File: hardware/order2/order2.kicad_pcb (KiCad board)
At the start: 2 copper layers, 377.8 x 228.9 mm, 183 parts, among them IC1 ATMEGA88-A, IC1 ATMEGA88A-A, J1 RJ45, J1 RJ45_8P8C_8FACH, K1 CONN_3, K1 pow_sel, K2 CONN_3, P1 CONN_4, P1 CONN_8, P1 ISP, P1 UART, P10 CONN_10, P11 CONN_8, P2 CONN_4, P2 CONN_6, P2 Shield, P2 UART, P2 so8, P3 CONN_4, P3 CONN_6, P3 i2c_pow, P4 CONN_8, P4 i2c_chain, P5 12Vin, P5 POW, P6 HOHLBUCHSE, P6 TWI, P7 TWI_POW, P7 Vccin, P8 CONN_10, P8 ISP, P9 5Vin, P9 CONN_8, SW1 SW1, SW1 SW_RESET, SW2 SCHALTER_2POL, SW3 SW_RESET, U1 LM7805, U1 ST485, U1 TSIC50XF, U2 HYT271, U2 ST485, U3 ST485, U4 ST485, U5 ST485, U6 ST485, U7 ST485, U8 ST485, U9 ST485, X1 20MHz, m3_loch VAL**

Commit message: humidity in place
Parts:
- moved C1 127.0 mm to (178.5, 119.6)
- moved C2 127.0 mm to (193.5, 132.5)
- moved C3 127.0 mm to (180.5, 135.8)
- moved C4 127.0 mm to (193.5, 135.5)
- moved C5 127.0 mm to (187.0, 141.0)
- moved C6 127.0 mm to (179.0, 103.0)
- moved D1 127.0 mm to (192.5, 112.9)
- moved IC1 127.0 mm to (184.5, 114.5)
- moved J1 127.0 mm to (186.5, 153.5)
- moved P1 127.0 mm to (186.5, 125.5)
- moved P2 127.0 mm to (180.7, 105.1)
- moved R1 127.0 mm to (192.5, 117.5)
- moved R3 127.0 mm to (180.5, 132.2)
- moved R4 127.0 mm to (180.5, 138.8)
- moved R5 127.0 mm to (193.5, 138.5)
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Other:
- board size 377.8 x 228.9 mm -> 381.8 x 229.9 mm

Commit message: 2 temp boards
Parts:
- added C1: 100nF, SM0603_big, F.Cu at (315.2, 203.0)
- added C2: 100nF, SM0603_big, F.Cu at (329.8, 211.8)
- added C3: 10uF, SM0805_big, F.Cu at (329.8, 215.2)
- added C4: 100nF, SM0603_big, F.Cu at (324.2, 222.5)
- added J1: RJ45, RJ45_8P8_simple, F.Cu at (322.5, 228.5)
- added R1: 220, SM0603_big, F.Cu at (315.2, 207.0)
- added R2: 22k, SM0603_big, F.Cu at (325.0, 218.8)
- added R3: 22k, SM0603_big, F.Cu at (330.0, 218.8)
- added R4: 120, SM0603_big, F.Cu at (328.2, 222.5)
- added U1: TSIC50XF, Tsic_TO92, F.Cu at (322.5, 172.0)
- added U2: ST485, st485, F.Cu at (322.5, 212.8)
- added m3_loch: VAL**, m3_loch, F.Cu at (327.5, 204.2)
- added m3_loch: VAL**, m3_loch, F.Cu at (317.5, 220.2)
- moved K1 389.8 mm to (40.7, 269.5)
- moved K2 389.8 mm to (35.6, 269.5)
- moved P1 389.8 mm to (48.7, 235.3)
- moved P1 389.8 mm to (33.7, 236.3)
- moved P1 389.8 mm to (61.2, 266.3)
- moved P2 389.8 mm to (48.7, 230.9)
- moved P2 389.8 mm to (33.7, 231.9)
- moved P2 389.8 mm to (66.3, 266.3)
- moved P3 389.8 mm to (48.7, 222.6)
- moved P3 389.8 mm to (33.7, 223.6)
- moved C1 273.9 mm to (311.2, 73.5), turned to 270 degrees
- moved R1 273.4 mm to (311.2, 69.5), turned to 270 degrees
- moved U1 271.7 mm to (304.0, 104.5), turned to 0 degrees
- moved m3_loch 269.4 mm to (309.0, 56.2), turned to 90 degrees
- moved U2 262.7 mm to (304.0, 63.8), turned to 45 degrees
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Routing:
- net GND: track 1547.1 -> 1674.0 mm, vias 17 -> 19
- net VCC: track 1094.8 -> 1152.5 mm, vias 10 -> 13
- net N-000007: track 59.1 -> 104.6 mm
- net N-0000010: track 42.9 -> 82.4 mm
- net /zb: track 80.3 -> 105.2 mm
- net /za: track 82.4 -> 106.6 mm
- net N-000003: track 24.9 -> 27.0 mm
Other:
- board size 381.8 x 229.9 mm -> 312.5 x 247.6 mm

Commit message: 10 temp sensor work
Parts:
- added C1: 100nF, SM0603_big, F.Cu at (318.2, 68.5)
- added C1: 100nF, SM0603_big, F.Cu at (288.8, 79.5)
- added C1: 100nF, SM0603_big, F.Cu at (318.8, 79.5)
- added C1: 100nF, SM0603_big, F.Cu at (348.2, 68.5)
- added C1: 100nF, SM0603_big, F.Cu at (288.2, 68.5)
- added C1: 100nF, SM0603_big, F.Cu at (258.8, 79.5)
- added C1: 100nF, SM0603_big, F.Cu at (378.2, 68.5)
- added C1: 100nF, SM0603_big, F.Cu at (348.8, 79.5)
- added C2: 100nF, SM0603_big, F.Cu at (303.8, 59.8)
- added C2: 100nF, SM0603_big, F.Cu at (303.2, 88.2)
- added C2: 100nF, SM0603_big, F.Cu at (333.2, 88.2)
- added C2: 100nF, SM0603_big, F.Cu at (333.8, 59.8)
- added C2: 100nF, SM0603_big, F.Cu at (273.8, 59.8)
- added C2: 100nF, SM0603_big, F.Cu at (273.2, 88.2)
- added C2: 100nF, SM0603_big, F.Cu at (363.8, 59.8)
- added C2: 100nF, SM0603_big, F.Cu at (363.2, 88.2)
- added C3: 10uF, SM0805_big, F.Cu at (303.8, 56.2)
- added C3: 10uF, SM0805_big, F.Cu at (303.2, 91.8)
- added C3: 10uF, SM0805_big, F.Cu at (333.2, 91.8)
- added C3: 10uF, SM0805_big, F.Cu at (333.8, 56.2)
- added C3: 10uF, SM0805_big, F.Cu at (273.8, 56.2)
- added C3: 10uF, SM0805_big, F.Cu at (273.2, 91.8)
- added C3: 10uF, SM0805_big, F.Cu at (363.8, 56.2)
- added C3: 10uF, SM0805_big, F.Cu at (363.2, 91.8)
- added C4: 100nF, SM0603_big, F.Cu at (309.2, 49.0)
- added C4: 100nF, SM0603_big, F.Cu at (297.8, 99.0)
- added C4: 100nF, SM0603_big, F.Cu at (327.8, 99.0)
- added C4: 100nF, SM0603_big, F.Cu at (339.2, 49.0)
- added C4: 100nF, SM0603_big, F.Cu at (279.2, 49.0)
- added C4: 100nF, SM0603_big, F.Cu at (267.8, 99.0)
- added C4: 100nF, SM0603_big, F.Cu at (369.2, 49.0)
- added C4: 100nF, SM0603_big, F.Cu at (357.8, 99.0)
- added J1: RJ45, RJ45_8P8_simple, F.Cu at (311.0, 43.0)
- added J1: RJ45, RJ45_8P8_simple, F.Cu at (296.0, 105.0)
- added J1: RJ45, RJ45_8P8_simple, F.Cu at (326.0, 105.0)
- added J1: RJ45, RJ45_8P8_simple, F.Cu at (341.0, 43.0)
- added J1: RJ45, RJ45_8P8_simple, F.Cu at (281.0, 43.0)
- added J1: RJ45, RJ45_8P8_simple, F.Cu at (266.0, 105.0)
- added J1: RJ45, RJ45_8P8_simple, F.Cu at (371.0, 43.0)
- added J1: RJ45, RJ45_8P8_simple, F.Cu at (356.0, 105.0)
- added R1: 220, SM0603_big, F.Cu at (318.2, 64.5)
- added R1: 220, SM0603_big, F.Cu at (288.8, 83.5)
- added R1: 220, SM0603_big, F.Cu at (318.8, 83.5)
- added R1: 220, SM0603_big, F.Cu at (348.2, 64.5)
- added R1: 220, SM0603_big, F.Cu at (288.2, 64.5)
- added R1: 220, SM0603_big, F.Cu at (258.8, 83.5)
- added R1: 220, SM0603_big, F.Cu at (378.2, 64.5)
- added R1: 220, SM0603_big, F.Cu at (348.8, 83.5)
- added R2: 22k, SM0603_big, F.Cu at (308.5, 52.8)
- added R2: 22k, SM0603_big, F.Cu at (298.5, 95.2)
- added R2: 22k, SM0603_big, F.Cu at (328.5, 95.2)
- added R2: 22k, SM0603_big, F.Cu at (338.5, 52.8)
- added R2: 22k, SM0603_big, F.Cu at (278.5, 52.8)
- added R2: 22k, SM0603_big, F.Cu at (268.5, 95.2)
- added R2: 22k, SM0603_big, F.Cu at (368.5, 52.8)
- added R2: 22k, SM0603_big, F.Cu at (358.5, 95.2)
- added R3: 22k, SM0603_big, F.Cu at (303.5, 52.8)
- added R3: 22k, SM0603_big, F.Cu at (303.5, 95.2)
- added R3: 22k, SM0603_big, F.Cu at (333.5, 95.2)
- added R3: 22k, SM0603_big, F.Cu at (333.5, 52.8)
- added R3: 22k, SM0603_big, F.Cu at (273.5, 52.8)
- added R3: 22k, SM0603_big, F.Cu at (273.5, 95.2)
- added R3: 22k, SM0603_big, F.Cu at (363.5, 52.8)
- added R3: 22k, SM0603_big, F.Cu at (363.5, 95.2)
- added R4: 120, SM0603_big, F.Cu at (305.2, 49.0)
- added R4: 120, SM0603_big, F.Cu at (301.8, 99.0)
- added R4: 120, SM0603_big, F.Cu at (331.8, 99.0)
- added R4: 120, SM0603_big, F.Cu at (335.2, 49.0)
- added R4: 120, SM0603_big, F.Cu at (275.2, 49.0)
- added R4: 120, SM0603_big, F.Cu at (271.8, 99.0)
- added R4: 120, SM0603_big, F.Cu at (365.2, 49.0)
- added R4: 120, SM0603_big, F.Cu at (361.8, 99.0)
- added U1: TSIC50XF, Tsic_TO92, F.Cu at (311.0, 99.5)
- added U1: TSIC50XF, Tsic_TO92, F.Cu at (296.0, 48.5)
- added U1: TSIC50XF, Tsic_TO92, F.Cu at (326.0, 48.5)
- added U1: TSIC50XF, Tsic_TO92, F.Cu at (341.0, 99.5)
- added U1: TSIC50XF, Tsic_TO92, F.Cu at (281.0, 99.5)
- added U1: TSIC50XF, Tsic_TO92, F.Cu at (266.0, 48.5)
- added U1: TSIC50XF, Tsic_TO92, F.Cu at (371.0, 99.5)
- added U1: TSIC50XF, Tsic_TO92, F.Cu at (356.0, 48.5)
- added U2: ST485, st485, F.Cu at (311.0, 58.8)
- added U2: ST485, st485, F.Cu at (296.0, 89.2)
- added U2: ST485, st485, F.Cu at (326.0, 89.2)
- added U2: ST485, st485, F.Cu at (341.0, 58.8)
- added U2: ST485, st485, F.Cu at (281.0, 58.8)
- added U2: ST485, st485, F.Cu at (266.0, 89.2)
- added U2: ST485, st485, F.Cu at (371.0, 58.8)
- added U2: ST485, st485, F.Cu at (356.0, 89.2)
- added m3_loch: VAL**, m3_loch, F.Cu at (306.0, 67.2)
- added m3_loch: VAL**, m3_loch, F.Cu at (286.0, 51.2)
- added m3_loch: VAL**, m3_loch, F.Cu at (261.0, 96.8)
- added m3_loch: VAL**, m3_loch, F.Cu at (271.0, 80.8)
- added m3_loch: VAL**, m3_loch, F.Cu at (366.0, 67.2)
- added m3_loch: VAL**, m3_loch, F.Cu at (376.0, 51.2)
- added m3_loch: VAL**, m3_loch, F.Cu at (351.0, 96.8)
- added m3_loch: VAL**, m3_loch, F.Cu at (361.0, 80.8)
- added m3_loch: VAL**, m3_loch, F.Cu at (316.0, 51.2)
- added m3_loch: VAL**, m3_loch, F.Cu at (291.0, 96.8)
- added m3_loch: VAL**, m3_loch, F.Cu at (301.0, 80.8)
- added m3_loch: VAL**, m3_loch, F.Cu at (331.0, 80.8)
- added m3_loch: VAL**, m3_loch, F.Cu at (321.0, 96.8)
- added m3_loch: VAL**, m3_loch, F.Cu at (346.0, 51.2)
- added m3_loch: VAL**, m3_loch, F.Cu at (336.0, 67.2)
- added m3_loch: VAL**, m3_loch, F.Cu at (276.0, 67.2)
- moved C1 150.8 mm to (228.8, 79.5)
- moved C2 150.8 mm to (243.2, 88.2)
- moved C3 150.8 mm to (243.2, 91.8)
- moved C4 150.8 mm to (237.8, 99.0)
- moved J1 150.8 mm to (236.0, 105.0)
- moved R1 150.8 mm to (228.8, 83.5)
- moved R2 150.8 mm to (238.5, 95.2)
- moved R3 150.8 mm to (243.5, 95.2)
- moved R4 150.8 mm to (241.8, 99.0)
- moved U1 150.8 mm to (236.0, 48.5)
- moved U2 150.8 mm to (236.0, 89.2)
- moved m3_loch 150.8 mm to (241.0, 80.8)
- moved m3_loch 150.8 mm to (231.0, 96.8)
- moved C1 53.2 mm to (258.2, 68.5)
- moved C2 53.2 mm to (243.8, 59.8)
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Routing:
- net GND: track 1674.0 -> 2688.7 mm, vias 19 -> 35
- net VCC: track 1152.5 -> 1613.9 mm, vias 13 -> 37
- net N-000007: track 104.6 -> 468.9 mm
- net N-0000010: track 82.4 -> 398.4 mm
- net /zb: track 105.2 -> 304.7 mm
- net /za: track 106.6 -> 299.5 mm
- net N-000003: track 27.0 -> 43.9 mm
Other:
- board size 312.5 x 247.6 mm -> 361 x 247.6 mm

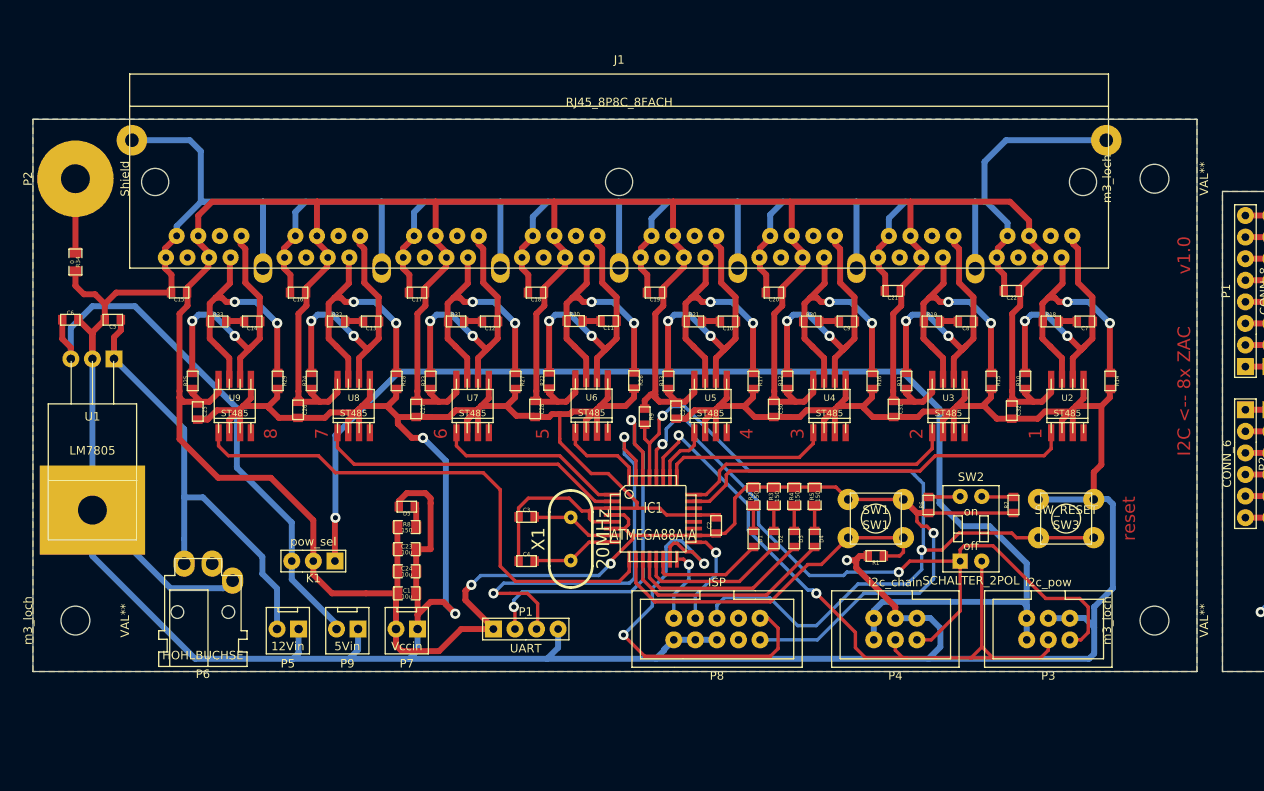
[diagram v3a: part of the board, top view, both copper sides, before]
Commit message: sensor board rotated
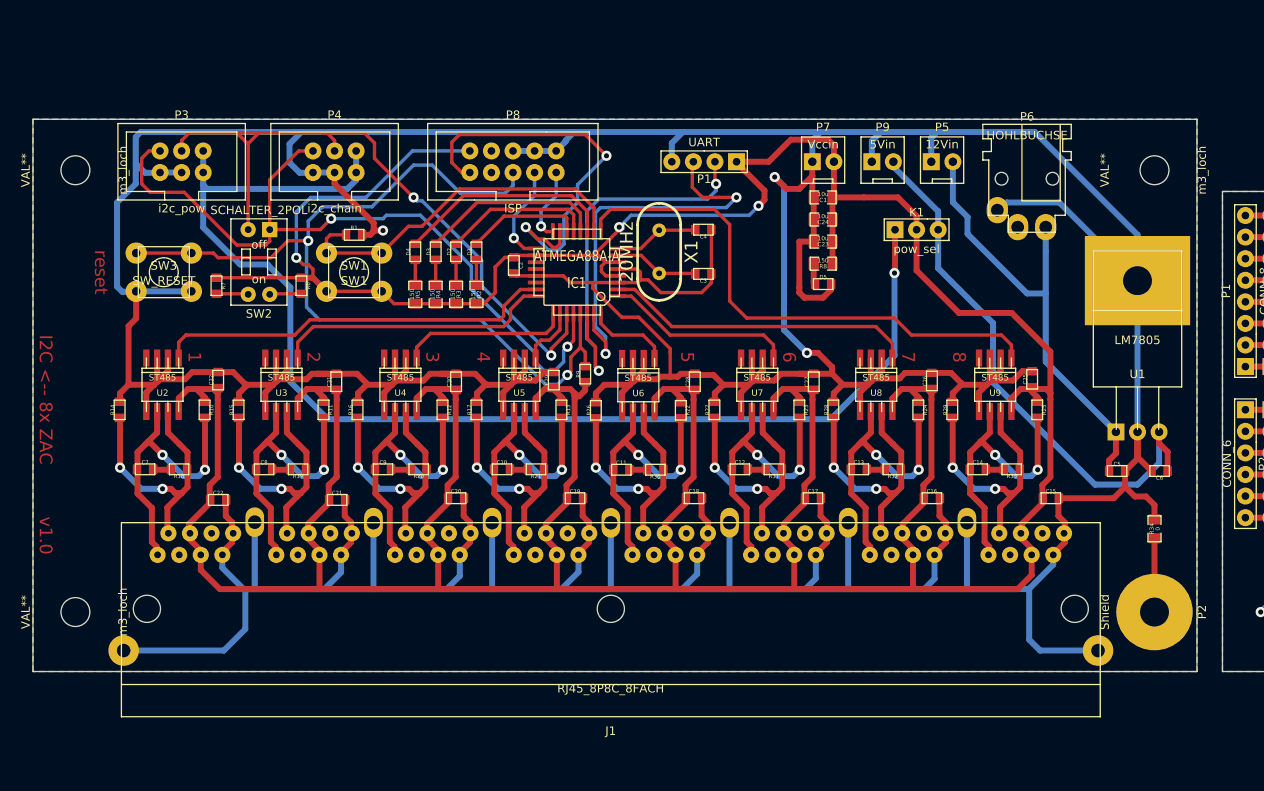
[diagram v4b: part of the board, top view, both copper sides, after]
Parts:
- moved m3_loch 137.6 mm to (25.0, 126.0), turned to 270 degrees
- moved m3_loch 137.6 mm to (152.0, 126.0), turned to 270 degrees
- moved P2 136.9 mm to (152.0, 178.0), turned to 270 degrees
- moved m3_loch 136.9 mm to (25.0, 178.0), turned to 270 degrees
- moved R34 130.8 mm to (152.0, 168.2), turned to 90 degrees
- moved C6 129.4 mm to (152.6, 161.4), turned to 180 degrees
- moved U1 125.9 mm to (150.0, 139.0), turned to 0 degrees
- moved C5 119.5 mm to (147.6, 161.4), turned to 0 degrees
- moved R14 116.6 mm to (30.2, 154.2), turned to 90 degrees
- moved P3 115.9 mm to (37.5, 125.0), turned to 0 degrees
- moved C7 112.0 mm to (33.2, 161.2), turned to 0 degrees
- moved SW3 110.1 mm to (35.4, 138.0), turned to 0 degrees
- moved P6 109.6 mm to (137.0, 127.0), turned to 0 degrees
- moved U2 106.5 mm to (35.2, 153.2), turned to 180 degrees
- moved C15 105.4 mm to (139.8, 164.6), turned to 0 degrees
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
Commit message: einzeln
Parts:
- removed the C1 at (318.2, 68.5)
- removed the C1 at (288.8, 79.5)
- removed the C1 at (318.8, 79.5)
- removed the C1 at (348.2, 68.5)
- removed the C1 at (288.2, 68.5)
- removed the C1 at (258.8, 79.5)
- removed the C1 at (378.2, 68.5)
- removed the C1 at (348.8, 79.5)
- removed the C2 at (303.8, 59.8)
- removed the C2 at (303.2, 88.2)
- removed the C2 at (333.2, 88.2)
- removed the C2 at (333.8, 59.8)
- removed the C2 at (273.8, 59.8)
- removed the C2 at (273.2, 88.2)
- removed the C2 at (363.8, 59.8)
- removed the C2 at (363.2, 88.2)
- removed the C3 at (303.8, 56.2)
- removed the C3 at (303.2, 91.8)
- removed the C3 at (333.2, 91.8)
- removed the C3 at (333.8, 56.2)
- removed the C3 at (273.8, 56.2)
- removed the C3 at (273.2, 91.8)
- removed the C3 at (363.8, 56.2)
- removed the C3 at (363.2, 91.8)
- removed the C4 at (309.2, 49.0)
- removed the C4 at (297.8, 99.0)
- removed the C4 at (327.8, 99.0)
- removed the C4 at (339.2, 49.0)
- removed the C4 at (279.2, 49.0)
- removed the C4 at (267.8, 99.0)
- removed the C4 at (369.2, 49.0)
- removed the C4 at (357.8, 99.0)
- removed the J1 at (311.0, 43.0)
- removed the J1 at (296.0, 105.0)
- removed the J1 at (326.0, 105.0)
- removed the J1 at (341.0, 43.0)
- removed the J1 at (281.0, 43.0)
- removed the J1 at (266.0, 105.0)
- removed the J1 at (371.0, 43.0)
- removed the J1 at (356.0, 105.0)
- removed the R1 at (318.2, 64.5)
- removed the R1 at (288.8, 83.5)
- removed the R1 at (318.8, 83.5)
- removed the R1 at (348.2, 64.5)
- removed the R1 at (288.2, 64.5)
- removed the R1 at (258.8, 83.5)
- removed the R1 at (378.2, 64.5)
- removed the R1 at (348.8, 83.5)
- removed the R2 at (308.5, 52.8)
- removed the R2 at (298.5, 95.2)
- removed the R2 at (328.5, 95.2)
- removed the R2 at (338.5, 52.8)
- removed the R2 at (278.5, 52.8)
- removed the R2 at (268.5, 95.2)
- removed the R2 at (368.5, 52.8)
- removed the R2 at (358.5, 95.2)
- removed the R3 at (303.5, 52.8)
- removed the R3 at (303.5, 95.2)
- removed the R3 at (333.5, 95.2)
- removed the R3 at (333.5, 52.8)
- removed the R3 at (273.5, 52.8)
- removed the R3 at (273.5, 95.2)
- removed the R3 at (363.5, 52.8)
- removed the R3 at (363.5, 95.2)
- removed the R4 at (305.2, 49.0)
- removed the R4 at (301.8, 99.0)
- removed the R4 at (331.8, 99.0)
- removed the R4 at (335.2, 49.0)
- removed the R4 at (275.2, 49.0)
- removed the R4 at (271.8, 99.0)
- removed the R4 at (365.2, 49.0)
- removed the R4 at (361.8, 99.0)
- removed the U1 at (311.0, 99.5)
- removed the U1 at (296.0, 48.5)
- removed the U1 at (326.0, 48.5)
- removed the U1 at (341.0, 99.5)
- removed the U1 at (281.0, 99.5)
- removed the U1 at (266.0, 48.5)
- removed the U1 at (371.0, 99.5)
- removed the U1 at (356.0, 48.5)
- removed the U2 at (311.0, 58.8)
- removed the U2 at (296.0, 89.2)
- removed the U2 at (326.0, 89.2)
- removed the U2 at (341.0, 58.8)
- removed the U2 at (281.0, 58.8)
- removed the U2 at (266.0, 89.2)
- removed the U2 at (371.0, 58.8)
- removed the U2 at (356.0, 89.2)
- removed the m3_loch at (306.0, 67.2)
- removed the m3_loch at (286.0, 51.2)
- removed the m3_loch at (261.0, 96.8)
- removed the m3_loch at (271.0, 80.8)
- removed the m3_loch at (366.0, 67.2)
- removed the m3_loch at (376.0, 51.2)
- removed the m3_loch at (351.0, 96.8)
- removed the m3_loch at (361.0, 80.8)
- removed the m3_loch at (316.0, 51.2)
- removed the m3_loch at (291.0, 96.8)
- removed the m3_loch at (301.0, 80.8)
- removed the m3_loch at (331.0, 80.8)
- removed the m3_loch at (321.0, 96.8)
- removed the m3_loch at (346.0, 51.2)
- removed the m3_loch at (336.0, 67.2)
- removed the m3_loch at (276.0, 67.2)
- added C1: 100nF, SM0603_big, F.Cu at (181.2, 63.5)
- added C1: 100nF, SM0603_big, F.Cu at (151.8, 74.5)
- added C2: 100nF, SM0603_big, F.Cu at (166.8, 54.8)
- added C2: 100nF, SM0603_big, F.Cu at (166.2, 83.2)
- added C3: 10uF, SM0805_big, F.Cu at (166.8, 51.2)
- added C3: 10uF, SM0805_big, F.Cu at (166.2, 86.8)
- added C4: 100nF, SM0603_big, F.Cu at (172.2, 44.0)
- added C4: 100nF, SM0603_big, F.Cu at (160.8, 94.0)
- added J1: RJ45, RJ45_8P8_simple, F.Cu at (174.0, 38.0)
- added J1: RJ45, RJ45_8P8_simple, F.Cu at (159.0, 100.0)
- added R1: 220, SM0603_big, F.Cu at (181.2, 59.5)
- added R1: 220, SM0603_big, F.Cu at (151.8, 78.5)
- added R2: 22k, SM0603_big, F.Cu at (171.5, 47.8)
- added R2: 22k, SM0603_big, F.Cu at (161.5, 90.2)
- added R3: 22k, SM0603_big, F.Cu at (166.5, 47.8)
- added R3: 22k, SM0603_big, F.Cu at (166.5, 90.2)
- added R4: 120, SM0603_big, F.Cu at (168.2, 44.0)
- added R4: 120, SM0603_big, F.Cu at (164.8, 94.0)
- added U1: TSIC50XF, Tsic_TO92, F.Cu at (174.0, 94.5)
- added U1: TSIC50XF, Tsic_TO92, F.Cu at (159.0, 43.5)
- added U2: ST485, st485, F.Cu at (174.0, 53.8)
- added U2: ST485, st485, F.Cu at (159.0, 84.2)
- added m3_loch: VAL**, m3_loch, F.Cu at (169.0, 62.2)
- added m3_loch: VAL**, m3_loch, F.Cu at (179.0, 46.2)
- added m3_loch: VAL**, m3_loch, F.Cu at (154.0, 91.8)
- added m3_loch: VAL**, m3_loch, F.Cu at (164.0, 75.8)
- moved C1 69.1 mm to (297.8, 82.5)
- moved C1 69.1 mm to (327.2, 71.5)
- moved C2 69.1 mm to (312.2, 91.2)
- moved C2 69.1 mm to (312.8, 62.8)
- moved C3 69.1 mm to (312.2, 94.8)
- moved C3 69.1 mm to (312.8, 59.2)
- moved C4 69.1 mm to (306.8, 102.0)
- moved C4 69.1 mm to (318.2, 52.0)
- moved J1 69.1 mm to (305.0, 108.0)
- moved J1 69.1 mm to (320.0, 46.0)
- moved R1 69.1 mm to (297.8, 86.5)
- moved R1 69.1 mm to (327.2, 67.5)
- moved R2 69.1 mm to (307.5, 98.2)
- moved R2 69.1 mm to (317.5, 55.8)
- moved R3 69.1 mm to (312.5, 98.2)
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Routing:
- net GND: track 2688.7 -> 1927.7 mm, vias 35 -> 23
- net VCC: track 1613.9 -> 1267.8 mm, vias 37 -> 19
- net N-000007: track 468.9 -> 195.7 mm
- net N-0000010: track 398.4 -> 161.4 mm
- net /zb: track 304.7 -> 155.1 mm
- net /za: track 299.5 -> 154.8 mm
- net N-000003: track 43.9 -> 31.2 mm
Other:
- board size 361 x 247.6 mm -> 310 x 251.6 mm
